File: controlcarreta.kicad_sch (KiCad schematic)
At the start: 92 parts, among them J1 Screw_Terminal_01x02, J10 MOLEX10POS, J11 MOLEX10POS, J1255 Conn_Coaxial, J13 USB_C_Receptacle_USB2.0_16P, J14 EG25-G / SIM7600G-H (Mini PCI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, J15 nano-SIM, J16 u.FL, J17 RS-232 DE9 (M, DTE), J2 Screw_Terminal_01x02, J3 Conn_01x04_Male, J4 MOLEX10POS, J5 MOLEX10POS, J6 MOLEX10POS, J7 MOLEX10POS, J8 MOLEX10POS, J9 MOLEX10POS, Q1 SI4447ADY-T1-GE3, SW1 SW_Push, SW2 SW_Push, U1 ESP32-S3-WROOM-1-N8, U10 LM2596S-ADJ, U11 MAX3232, U2 LM2596S-ADJ, U3 sdcard, U4 74LVC8T245PW, U5 74LVC8T245PW, U6 74LVC8T245PW, U8 NCP1117-3.3, U9 USBLC6-2SC6

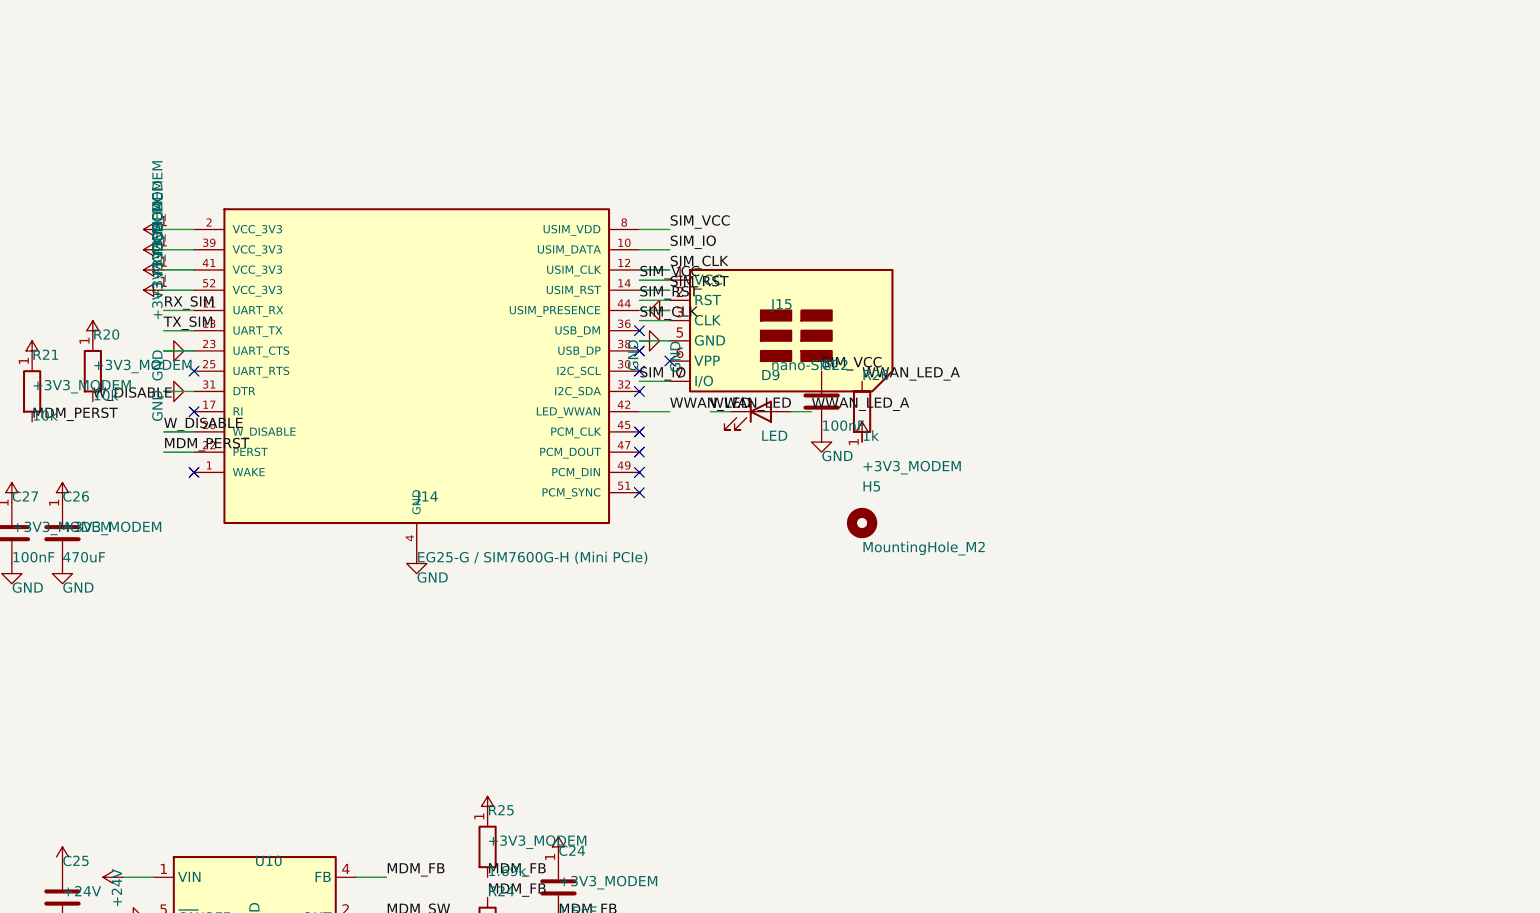
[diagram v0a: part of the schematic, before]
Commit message: J14: zocalo Mini PCIe con footprint/simbolo estandar de KiCad
- Simbolo: Connector:Bus_PCI_Express_Mini  (antes: simbolo propio MINI_PCIE_52,
  inventado).
- Footprint: Connector_PCBEdge:BUS_PCI_Express_Mini_Full  (zocalo Mini PCIe 52p
  real; antes un nombre inventado que no existia).
- H5 -> Connector_PCBEdge:JAE_MM60-EZH039-Bx_BUS_PCI_Express_Holder (retencion).
- R27 (0 ohm) nuevo: pin 23 (UART_CTS del modem) -> GND. El pin es tipo
  'output' en el simbolo estandar, atarlo directo a GND daba error ERC.
- MINI_PCIE_52 eliminado de controlcarreta.kicad_sym.
- El cableado se mantiene por numero de pin (mapa en ESP32-S3-MIGRATION.md).
- collect_3d.py: ahora lee los footprints del esquematico; el modelo del
  zocalo Mini PCIe queda como ${KICAD9_3DMODEL_DIR}/... (viene en
  kicad-packages3d completo, esta maquina lo tiene incompleto).

ERC: 0 errores. Netlist: solo cambia J14/R27/H5, el resto identico.

Co-Authored-By: Claude Sonnet 5 <noreply@anthropic.com>
Claude-Session: https://claude.ai/code/session_011V2GTHvqBgNdus4vsEVVnA
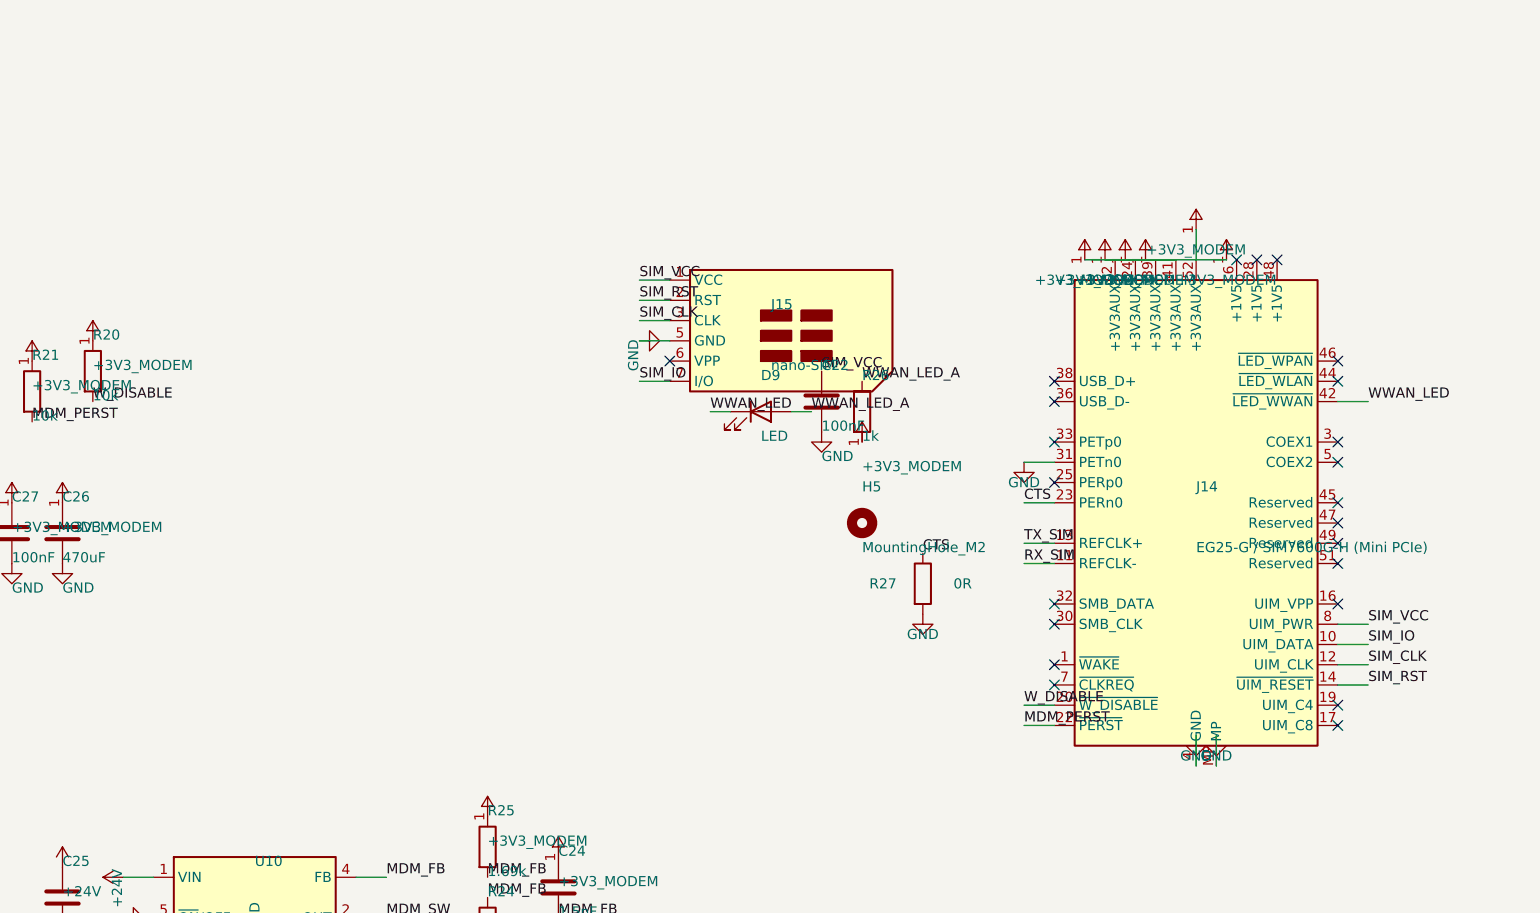
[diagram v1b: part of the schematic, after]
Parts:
- removed J14: EG25-G / SIM7600G-H (Mini PCIe), Connector_PCBEdge:mini_PCIe_Molex_679100000, symbol controlcarreta:MINI_PCIE_52
- added J14: EG25-G / SIM7600G-H (Mini PCIe), Connector_PCBEdge:BUS_PCI_Express_Mini_Full, symbol Connector:Bus_PCI_Express_Mini
- added R27: 0R, Resistor_SMD:R_1206_3216Metric_Pad1.30x1.75mm_HandSolder, symbol Device:R
- H5: footprint MountingHole:MountingHole_2.2mm_M2 -> Connector_PCBEdge:JAE_MM60-EZH039-Bx_BUS_PCI_Express_Holder
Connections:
- net +3V3_MODEM: now also J14.2 (+3V3AUX), J14.24 (+3V3AUX), J14.39 (+3V3AUX), J14.41 (+3V3AUX), J14.52 (+3V3AUX)
- net GND: now also J14.15 (GND), J14.18 (GND), J14.21 (GND), J14.26 (GND), J14.27 (GND), J14.29 (GND), J14.31 (PETn0), J14.34 (GND), J14.35 (GND), J14.37 (GND), J14.4 (GND), J14.40 (GND), J14.43 (GND), J14.50 (GND), J14.9 (GND), J14.MP, R27.2
- net MDM_PERST: now also J14.22 (~{PERST})
- net RX_SIM: now also J14.11 (REFCLK-)
- net SIM_CLK: now also J14.12 (UIM_CLK)
- net SIM_IO: now also J14.10 (UIM_DATA)
- net SIM_RST: now also J14.14 (~{UIM_RESET})
- net SIM_VCC: now also J14.8 (UIM_PWR)
- net TX_SIM: now also J14.13 (REFCLK+)
- net WWAN_LED: now also J14.42 (~{LED_WWAN})
- net W_DISABLE: now also J14.20 (~{W_DISABLE})
- new net CTS: J14.23 (PERn0), R27.1
- no-connect marks 80 -> 91

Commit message: U4/U5/U6: 74LVC8T245PW -> version AEC-Q100 (grado automocion)
MPN/Value = 74LVC8T245PW-Q100J (Nexperia). Mismo chip, mismo footprint
TSSOP-24, drop-in; solo cambia el grado a AEC-Q100 (-40..+125 C), apropiado
para el uso en vehiculo. Anadidos campos MPN y MANUFACTURER, y Datasheet
apunta a la pagina de DigiKey del -Q100J.

Netlist identico (cambio solo de propiedades). ERC 0 errores.

Co-Authored-By: Claude Sonnet 5 <noreply@anthropic.com>
Claude-Session: https://claude.ai/code/session_011V2GTHvqBgNdus4vsEVVnA
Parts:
- U4, U5, U6: value 74LVC8T245PW -> 74LVC8T245PW-Q100J; MANUFACTURER (none) -> Nexperia; MPN (none) -> 74LVC8T245PW-Q100J
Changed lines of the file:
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@@
 			)
 		)
-		(property "Value" "74LVC8T245PW"
+		(property "Value" "74LVC8T245PW-Q100J"
 			(at 156.6418 24.1554 0)
 			(effects
@@
 			)
 		)
-		(property "Datasheet" "https://www.digikey.com/es/products/detail/nexperia-usa-inc/74LVC8T245PW/13475248"
+		(property "Datasheet" "https://www.digikey.com/en/products/detail/nexperia-usa-inc/74LVC8T245PW-Q100J/4020317"
 			(at 145.415 26.035 0)
 			(effects
@@
 			)
 		)
+		(property "MPN" "74LVC8T245PW-Q100J"
+			(at 154.305 70.485 0)
+			(effects
+				(font
+					(size 1.27 1.27)
+				)
+				(justify left bottom)
+				(hide yes)
+			)
+		)
+		(property "MANUFACTURER" "Nexperia"
+			(at 154.305 70.485 0)
+			(effects
+				(font
+					(size 1.27 1.27)
+				)
+				(justify left bottom)
+				(hide yes)
+			)
+		)
 		(pin "1"
 		)
@@
 			)
 		)
-		(property "Value" "74LVC8T245PW"
+		(property "Value" "74LVC8T245PW-Q100J"
 			(at 156.0068 113.0554 0)
 			(effects
@@
 			)
 		)
-		(property "Datasheet" "https://www.digikey.com/es/products/detail/nexperia-usa-inc/74LVC8T245PW/13475248"
+		(property "Datasheet" "https://www.digikey.com/en/products/detail/nexperia-usa-inc/74LVC8T245PW-Q100J/4020317"
 			(at 144.78 114.935 0)
 			(effects
@@
 			)
 		)
+		(property "MPN" "74LVC8T245PW-Q100J"
+			(at 153.67 159.385 0)
+			(effects
+				(font
+					(size 1.27 1.27)
+				)
+				(justify left bottom)
+				(hide yes)
+			)
+		)
+		(property "MANUFACTURER" "Nexperia"
+			(at 153.67 159.385 0)
+			(effects
+				(font
+					(size 1.27 1.27)
+				)
+				(justify left bottom)
+				(hide yes)
+			)
+		)
 		(pin "1"
 		)
@@
 			)
 		)
-		(property "Value" "74LVC8T245PW"
+		(property "Value" "74LVC8T245PW-Q100J"
 			(at 156.0068 67.9704 0)
 			(effects
@@
 			)
 		)
-		(property "Datasheet" "https://www.digikey.com/es/products/detail/nexperia-usa-inc/74LVC8T245PW/13475248"
+		(property "Datasheet" "https://www.digikey.com/en/products/detail/nexperia-usa-inc/74LVC8T245PW-Q100J/4020317"
 			(at 144.78 69.85 0)
 			(effects
@@
 			)
 		)
+		(property "MPN" "74LVC8T245PW-Q100J"
+			(at 153.67 114.3 0)
+			(effects
+				(font
+					(size 1.27 1.27)
+				)
+				(justify left bottom)
+				(hide yes)
+			)
+		)
+		(property "MANUFACTURER" "Nexperia"
+			(at 153.67 114.3 0)
+			(effects
+				(font
+					(size 1.27 1.27)
+				)
+				(justify left bottom)
+				(hide yes)
+			)
+		)

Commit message: Esquematico: reorganizacion del layout (subsistemas nuevos sin solapes)
Reconstruye la disposicion de los ~40 componentes anadidos en la migracion
a ESP32-S3 (buck del modem, zocalo Mini PCIe J14, USB-C, RS-232) con un
floor plan por zonas. J14 vuelve a caer dentro de la hoja A3.

- Conectividad identica al commit anterior: el netlist coincide pin a pin,
  solo cambian posiciones.
- ERC: 0 errores.
- J14 +3V3AUX a un unico riel/simbolo; GND y MP consolidados.

Co-Authored-By: Claude Sonnet 5 <noreply@anthropic.com>
Claude-Session: https://claude.ai/code/session_011V2GTHvqBgNdus4vsEVVnA
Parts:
- D7, D8: MANUFACTURER (none) -> onsemi
- D9: value LED -> WWAN
- H5: value MountingHole_M2 -> MiniPCIe standoff
- J13: value USB_C_Receptacle_USB2.0_16P -> USB-C 2.0; MANUFACTURER (none) -> GCT; MPN (none) -> USB4085-GF-A
- J15: MANUFACTURER GCT -> CUI Devices; MPN SIM8060-6-1-14-00 -> NSIM-2-C
- J17: value RS-232 DE9 (M, DTE) -> RS-232 DE9 (M,DTE); MANUFACTURER Amphenol Cannon -> Amphenol; MPN L717SDE09PA4CH4RC30X -> L717SDE09PA4CH4F
- L2: MANUFACTURER (none) -> Bourns; MPN (none) -> SDR1806-330ML
- SW1: value SW_Push -> RESET; MANUFACTURER (none) -> Omron; MPN (none) -> B3F-1000
- SW2: value SW_Push -> BOOT; MANUFACTURER (none) -> Omron; MPN (none) -> B3F-1000
- U10: MANUFACTURER (none) -> Texas Instruments; MPN (none) -> LM2596S-ADJ/NOPB
- U9: MANUFACTURER (none) -> STMicroelectronics; MPN (none) -> USBLC6-2SC6

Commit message: J14: zocalo real JAE MM60-52B1-E1-R650 (en stock) en vez del modulo Quectel
El campo MPN/Datasheet de J14 apuntaba al modulo Quectel EG25GGB-MINIPCIE,
que no tiene stock. J14 es el ZOCALO Mini PCIe, no el modulo:

- MPN -> JAE MM60-52B1-E1-R650 (DigiKey Active, ~28k stock, ~1,65 US$),
  socket 52p 0,8mm con eyectores/latch integrados.
- Value -> "Mini PCIe Socket 52p". La tarjeta EG25-G/SIM7600G-H se inserta,
  no va en BOM (campo "Modulo" informativo).
- H5 eliminado: el MM60-E1 ya trae la retencion, no hace falta holder aparte.
- Footprint sin cambios (BUS_PCI_Express_Mini_Full = socket "with clips").
- Conectividad y ERC sin cambios (0 errores).

Co-Authored-By: Claude Sonnet 5 <noreply@anthropic.com>
Claude-Session: https://claude.ai/code/session_011V2GTHvqBgNdus4vsEVVnA
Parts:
- removed H5: MiniPCIe standoff, Connector_PCBEdge:JAE_MM60-EZH039-Bx_BUS_PCI_Express_Holder, symbol Mechanical:MountingHole
- J14: value EG25-G / SIM7600G-H (Mini PCIe) -> Mini PCIe Socket 52p; MANUFACTURER Quectel -> JAE Electronics; MPN EG25GGB-MINIPCIE -> MM60-52B1-E1-R650; Modulo (none) -> tarjeta EG25-G / SIM7600G-H (no va en BOM, se inserta)
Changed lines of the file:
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@@
 				)
 			)
-			(property "Value" "EG25-G / SIM7600G-H (Mini PCIe)"
+			(property "Value" "Mini PCIe Socket 52p"
 				(at 336.55 134.54 0)
 				(effects
@@
 				)
 			)
-			(property "Datasheet" "https://www.digikey.com/en/products/detail/quectel/EG25GGB-MINIPCIE/13278349"
+			(property "Datasheet" "https://www.digikey.com/en/products/detail/jae-electronics/MM60-52B1-E1-R650/2071034"
 				(at 336.55 129.54 0)
 				(effects
@@
 				)
 			)
-			(property "MPN" "EG25GGB-MINIPCIE"
+			(property "MPN" "MM60-52B1-E1-R650"
 				(at 336.55 129.54 0)
 				(effects
@@
 				)
 			)
-			(property "MANUFACTURER" "Quectel"
+			(property "MANUFACTURER" "JAE Electronics"
+				(at 336.55 129.54 0)
+				(effects
+					(font
+						(size 1.27 1.27)
+					)
+					(justify left bottom)
+					(hide yes)
+				)
+			)
+			(property "Modulo" "tarjeta EG25-G / SIM7600G-H (no va en BOM, se inserta)"
 				(at 336.55 129.54 0)
 				(effects
@@
 					(unit 1)
 				)
-			)
-		)
-	)
-	(symbol
-		(lib_id "Mechanical:MountingHole")
-		(at 299.72 218.44 0)
-		(unit 1)
-		(exclude_from_sim no)
-		(in_bom yes)
-		(on_board yes)
-		(dnp no)
-			(property "Reference" "H5"
-				(at 299.72 213.44 0)
-				(effects
-					(font
-						(size 1.27 1.27)
-					)
-					(justify left bottom)
-				)
-			)
-			(property "Value" "MiniPCIe standoff"
-				(at 299.72 223.44 0)
-				(effects
-					(font
-						(size 1.27 1.27)
-					)
-					(justify left bottom)
-				)
-			)
-			(property "Footprint" "Connector_PCBEdge:JAE_MM60-EZH039-Bx_BUS_PCI_Express_Holder"
-				(at 299.72 218.44 0)
-				(effects
-					(font
-						(size 1.27 1.27)
-					)
-					(justify left bottom)
-					(hide yes)
-				)
-			)
-			(property "Datasheet" "~"
-				(at 299.72 218.44 0)
-				(effects
-					(font
-						(size 1.27 1.27)
-					)
-					(justify left bottom)
-					(hide yes)
-				)
-			)
-			(property "Description" ""
-				(at 299.72 218.44 0)
-				(effects
-					(font
-						(size 1.27 1.27)
-					)
-					(justify left bottom)
-					(hide yes)
-				)
-			)
-		(instances
-			(project "controlcarreta"
-				(path "/9232987b-e923-413e-abd9-77ced6cc4c47"
-					(reference "H5")
-					(unit 1)
-				)

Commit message: U11: MAX3232IDR (obsoleto) -> MAX3232EIDR ; limpieza de MPNs sin stock
- U11: el MAX3232IDR esta "Obsolete and no longer manufactured". Cambiado al
  drop-in MAX3232EIDR (TI, Active, ~55k stock, mismo SOIC-16 y pinout, +-15kV ESD).
- U9: datasheet apuntaba a un clon Slkormicro; ahora al USBLC6-2SC6 de ST
  (Active, ~294k stock). Mismo MPN/footprint.
- J15: URL actualizada al listado vigente (CUI -> Same Sky), parte NSIM-2-C Active.
- Verificado el resto de piezas nuevas: LM2596S-ADJ/NOPB, NCP1117ST33T3G,
  USB4085-GF-A, JAE MM60-52B1-E1-R650 -> todas Active y con stock.
- Sin cambios de conectividad ni de ERC (0 errores).

Co-Authored-By: Claude Sonnet 5 <noreply@anthropic.com>
Claude-Session: https://claude.ai/code/session_011V2GTHvqBgNdus4vsEVVnA
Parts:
- J15: MANUFACTURER CUI Devices -> Same Sky (CUI Devices)
- U11: value MAX3232 -> MAX3232E; MPN MAX3232IDR -> MAX3232EIDR
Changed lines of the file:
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@@
 				)
 			)
-			(property "Datasheet" "https://www.digikey.com/en/products/detail/shenzhen-slkormicro-semicon-co-ltd/USBLC6-2SC6/28143029"
+			(property "Datasheet" "https://www.digikey.com/en/products/detail/stmicroelectronics/USBLC6-2SC6/1121688"
 				(at 208.28 246.38 0)
 				(effects
@@
 				)
 			)
-			(property "Value" "MAX3232"
+			(property "Value" "MAX3232E"
 				(at 270.51 251.38 0)
 				(effects
@@
 				)
 			)
-			(property "Datasheet" "https://www.digikey.com/en/products/detail/texas-instruments/MAX3232IDR/484759"
+			(property "Datasheet" "https://www.digikey.com/en/products/detail/texas-instruments/MAX3232EIDR/1089416"
 				(at 270.51 246.38 0)
 				(effects
@@
 				)
 			)
-			(property "MPN" "MAX3232IDR"
+			(property "MPN" "MAX3232EIDR"
 				(at 270.51 246.38 0)
 				(effects
@@
 				)
 			)
-			(property "Datasheet" "https://www.digikey.com/en/products/detail/cui-devices/NSIM-2-C/16585269"
+			(property "Datasheet" "https://www.digikey.com/en/products/detail/same-sky-formerly-cui-devices/NSIM-2-C/21796984"
 				(at 374.65 176.53 0)
 				(effects
@@
 				)
 			)
-			(property "MANUFACTURER" "CUI Devices"
+			(property "MANUFACTURER" "Same Sky (CUI Devices)"
 				(at 374.65 176.53 0)
 				(effects
